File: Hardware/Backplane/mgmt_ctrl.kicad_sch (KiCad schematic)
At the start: 16 parts, among them J501 Conn_01x03, U501 SN74LVC1G08DBVR, U502 CH32V003FxPx

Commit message: Adjusts to review comments
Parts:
- C501, C502, C503, C504: Digikey Part No (none) -> 399-C0603C104M4RACTUCT-ND
- J501: Digikey Part No (none) -> WM1732-ND
- R501: value 4K7 -> 10K; Digikey Part No (none) -> 311-10.0KHRCT-ND
- R502: value 6K8 -> 6K8 1%; Digikey Part No (none) -> RG16P6.8KBCT-ND
- R503, R507: value 1K8 -> 1K8 1%; Digikey Part No (none) -> RG16P1.8KBCT-ND
- R504, R505: value 2K7 -> 1K8 1%; Digikey Part No (none) -> RG16P1.8KBCT-ND
- R506: value 560 -> 560 1%; Digikey Part No (none) -> RR08P560DCT-ND
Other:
- moved on the sheet: C501

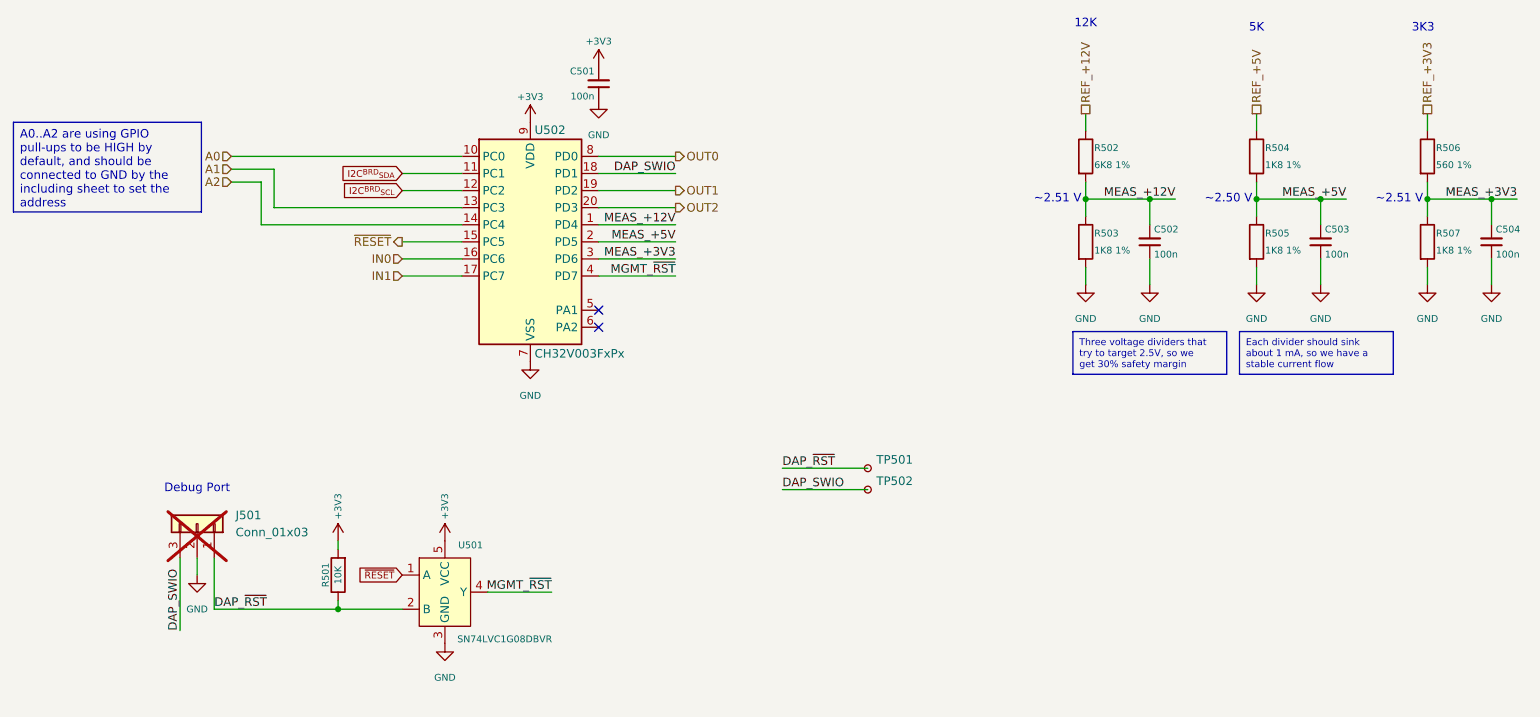
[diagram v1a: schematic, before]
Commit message: Starts refactoring Backplane to use NL17SZS11-D instead of 4-port AND
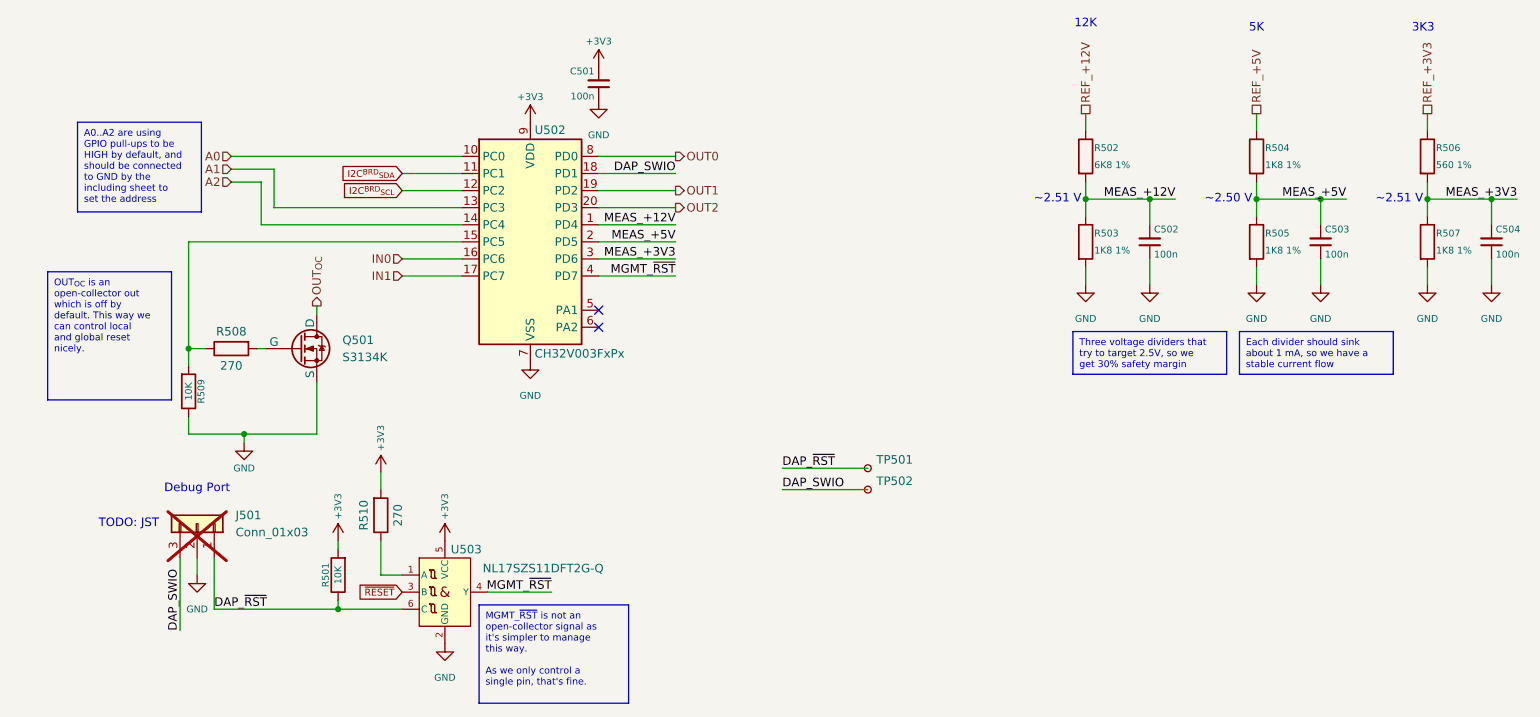
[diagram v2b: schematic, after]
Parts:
- removed U501: SN74LVC1G08DBVR, Package_TO_SOT_SMD:SOT-23-5, symbol Home Computer:SN74LVC1G08DBVR
- added Q501: S3134K, symbol Simulation_SPICE:NMOS
- added R508, R510: 270, Resistor_SMD:R_0603_1608Metric, symbol Device:R
- added R509: 10K, Resistor_SMD:R_0603_1608Metric, symbol Device:R
- added U503: NL17SZS11DFT2G-Q, Package_TO_SOT_SMD:SOT-363_SC-70-6, symbol Home Computer:NL17SZS11DFT2G-Q
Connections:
- net +3V3: now also R510.2, U503.5 (VCC)
- net DAP_~{RST}: now also U503.6 (C)
- net GND: now also Q501.3 (S), R509.1, U503.2 (GND)
- net MGMT_~{RST}: now also U503.4 (Y)
- net ~{RESET}: now also U503.3 (B); no longer U502.15 (PC5)
- new net: Q501.2 (G), R508.2
- new net: R510.1, U503.1 (A)
- new net: R508.1, R509.2, U502.15 (PC5)
- new net OUT_{OC}: Q501.1 (D)
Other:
- note added: "TODO: JST"

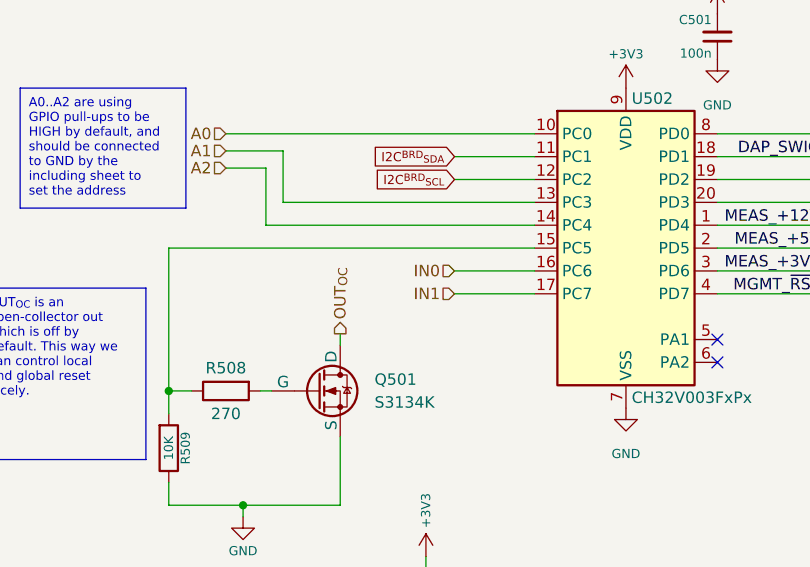
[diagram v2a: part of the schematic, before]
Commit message: Cleans up Backplane schematic even more. Less parts in the BOM, less mistakes!
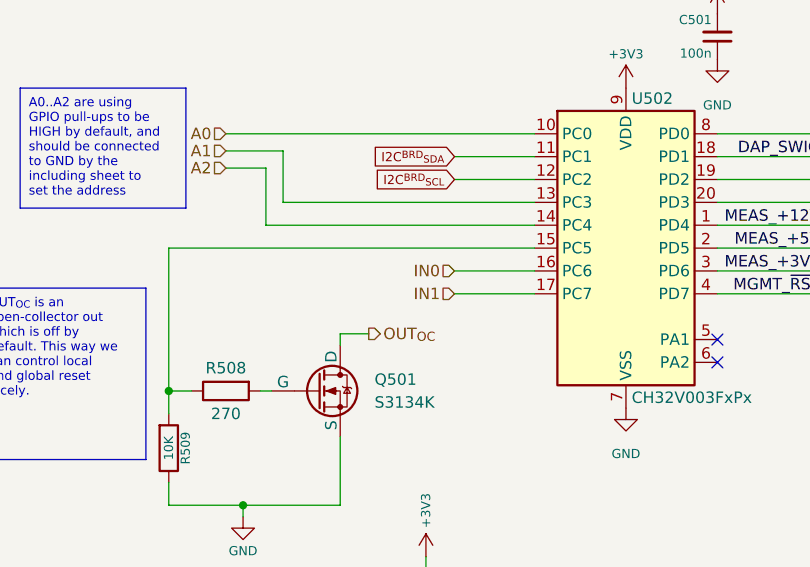
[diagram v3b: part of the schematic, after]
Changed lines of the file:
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@@
+	(wire
+		(pts
+			(xy 63.5 60.325) (xy 66.675 60.325)
+		)
+		(stroke
+			(width 0)
+			(type default)
+		)
+	)
 	(wire
 		(pts
@@
 	(hierarchical_label "OUT_{OC}"
 		(shape output)
-		(at 63.5 60.325 90)
-		(effects
-			(font
+		(at 66.675 60.325 0)
+		(effects
+			(font

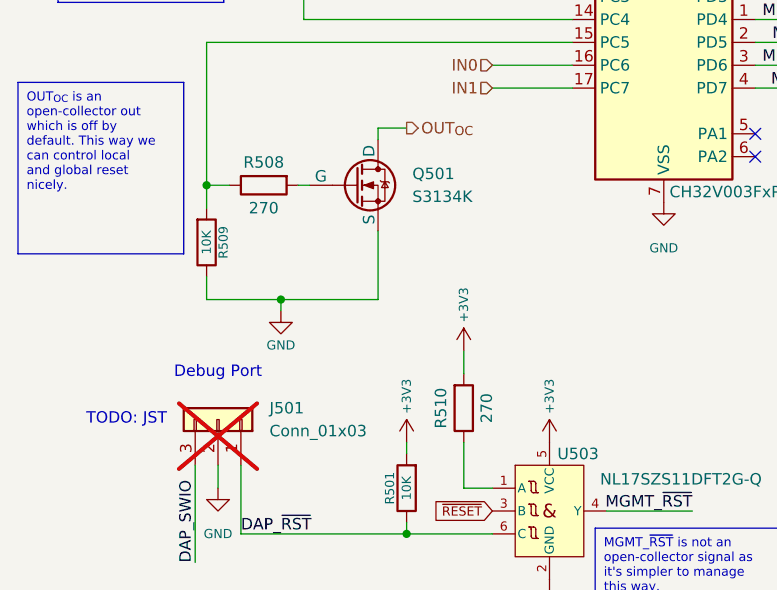
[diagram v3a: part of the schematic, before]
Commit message: Cleans up schematic even more, consolidates 270 and 100 Ohm resistors into the 560 ohm resistor, as they were only used as series resistors for the mosfets and LED current limiters
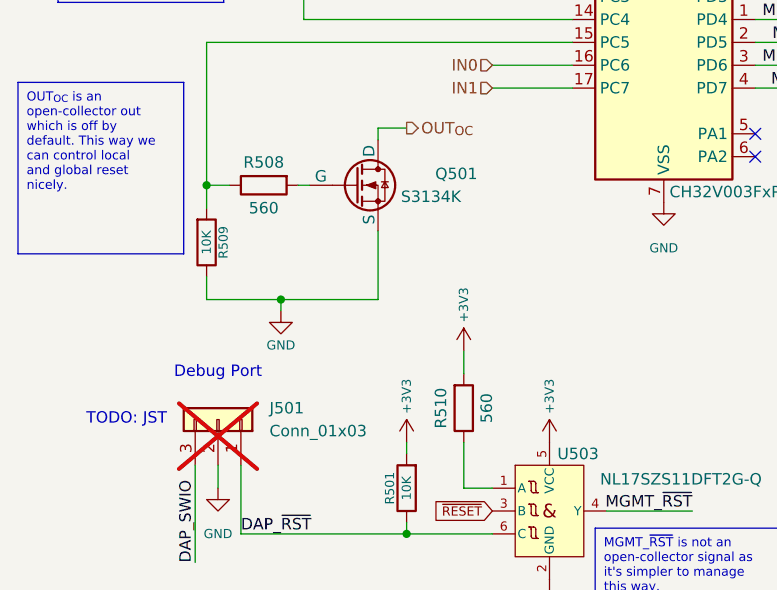
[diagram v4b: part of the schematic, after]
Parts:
- Q501: footprint (none) -> Package_TO_SOT_SMD:SOT-23; symbol Simulation_SPICE:NMOS -> Home Computer:S3134K
- R508, R510: value 270 -> 560; Digikey Part No RMCF0603FT270RCT-ND -> RR08P560DCT-ND
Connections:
- net GND: now also Q501.2 (S); no longer Q501.3 (S)
- net OUT_{OC}: now also Q501.3 (D); no longer Q501.1 (D)
- net at R508.2: now also Q501.1 (G); no longer Q501.2 (G)
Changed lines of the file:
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@@
 	)
 	(symbol
-		(lib_id "Simulation_SPICE:NMOS")
-		(at 60.96 66.675 0)
+		(lib_id "Home Computer:S3134K")
+		(at 63.5 66.675 0)
 		(unit 1)
 		(exclude_from_sim no)
@@
 		(dnp no)
 		(property "Reference" "Q501"
-			(at 67.31 65.4049 0)
+			(at 69.85 65.4049 0)
 			(effects
 				(font
@@
 		)
 		(property "Value" "S3134K"
-			(at 67.31 67.9449 0)
+			(at 66.04 67.945 0)
 			(effects
 				(font
@@
 			)
 		)
-		(property "Footprint" ""
-			(at 66.04 64.135 0)
+		(property "Footprint" "Package_TO_SOT_SMD:SOT-23"
+			(at 86.36 49.911 0)
 			(effects
 				(font
@@
 		)
 		(property "Datasheet" "https://goodarksemi.com/docs/datasheets/mosfets/S3134K.pdf"
-			(at 60.96 79.375 0)
+			(at 57.15 47.371 0)
 			(effects
 				(font
@@
 		)
 		(property "Description" "20V N-Channel MOSFET"
-			(at 60.96 66.675 0)
+			(at 84.328 79.375 0)
 			(effects
 				(font
@@
 		)
 		(property "Digikey Part No" "4786-S3134KCT-ND"
-			(at 60.96 66.675 0)
-			(effects
-				(font
-					(size 1.27 1.27)
+			(at 63.5 66.675 0)
+			(effects
+				(font
+					(size 1.016 1.016)
 				)
 				(hide yes)
@@
 			)
 		)
-		(property "Value" "270"
+		(property "Value" "560"
 			(at 50.8 69.215 90)
 			(effects
@@
 			)
 		)
-		(property "Datasheet" "https://www.seielect.com/catalog/SEI-RMCF_RMCP.pdf"
+		(property "Datasheet" "https://www.susumu.co.jp/common/pdf/n_catalog_partition05_en.pdf"
 			(at 50.8 66.675 0)
 			(effects
@@
 			)
 		)
-		(property "Digikey Part No" "RMCF0603FT270RCT-ND"
+		(property "Digikey Part No" "RR08P560DCT-ND"
 			(at 50.8 66.675 90)
 			(effects
@@
 			)
 		)
-		(property "Value" "270"
+		(property "Value" "560"
 			(at 75.565 91.44 90)
 			(effects
@@
 			)
 		)
-		(property "Datasheet" "https://www.seielect.com/catalog/SEI-RMCF_RMCP.pdf"
+		(property "Datasheet" "https://www.susumu.co.jp/common/pdf/n_catalog_partition05_en.pdf"
 			(at 73.025 91.44 0)
 			(effects
@@
 			)
 		)
-		(property "Digikey Part No" "RMCF0603FT270RCT-ND"
+		(property "Digikey Part No" "RR08P560DCT-ND"
 			(at 73.025 91.44 90)
 			(effects

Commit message: Upgrades schematic files to KiCAD 10.0
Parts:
- U503: DigiKey Part No 488-NL17SZS11DFT2G-QCT-ND -> (none); Digikey Part No (none) -> 488-NL17SZS11DFT2G-QCT-ND

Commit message: Further backplane PCB cleanup.
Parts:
- added TP2005, TP2013, TP2021: TestPoint_Small, TestPoint:TestPoint_Pad_D1.0mm, symbol Connector:TestPoint_Small
- J501: value Conn_01x03 -> BM03B-SRSS-TB; footprint Connector_Molex:Molex_PicoBlade_53047-0310_1x03_P1.25mm_Vertical -> Connector_JST:JST_SH_BM03B-SRSS-TB_1x03-1MP_P1.00mm_Vertical; Digikey Part No WM1732-ND -> 455-BM03B-SRSS-TBTR-ND
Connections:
- net MEAS_+12V: now also TP2005.1
- net MEAS_+3V3: now also TP2021.1
- net MEAS_+5V: now also TP2013.1
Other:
- note removed: "TODO: JST"
- moved on the sheet: TP501, TP502
